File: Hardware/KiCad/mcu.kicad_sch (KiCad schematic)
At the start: 9 parts, among them U3 STM32F427ZGTx, Y1 8 MHz, Y2 32 kHz

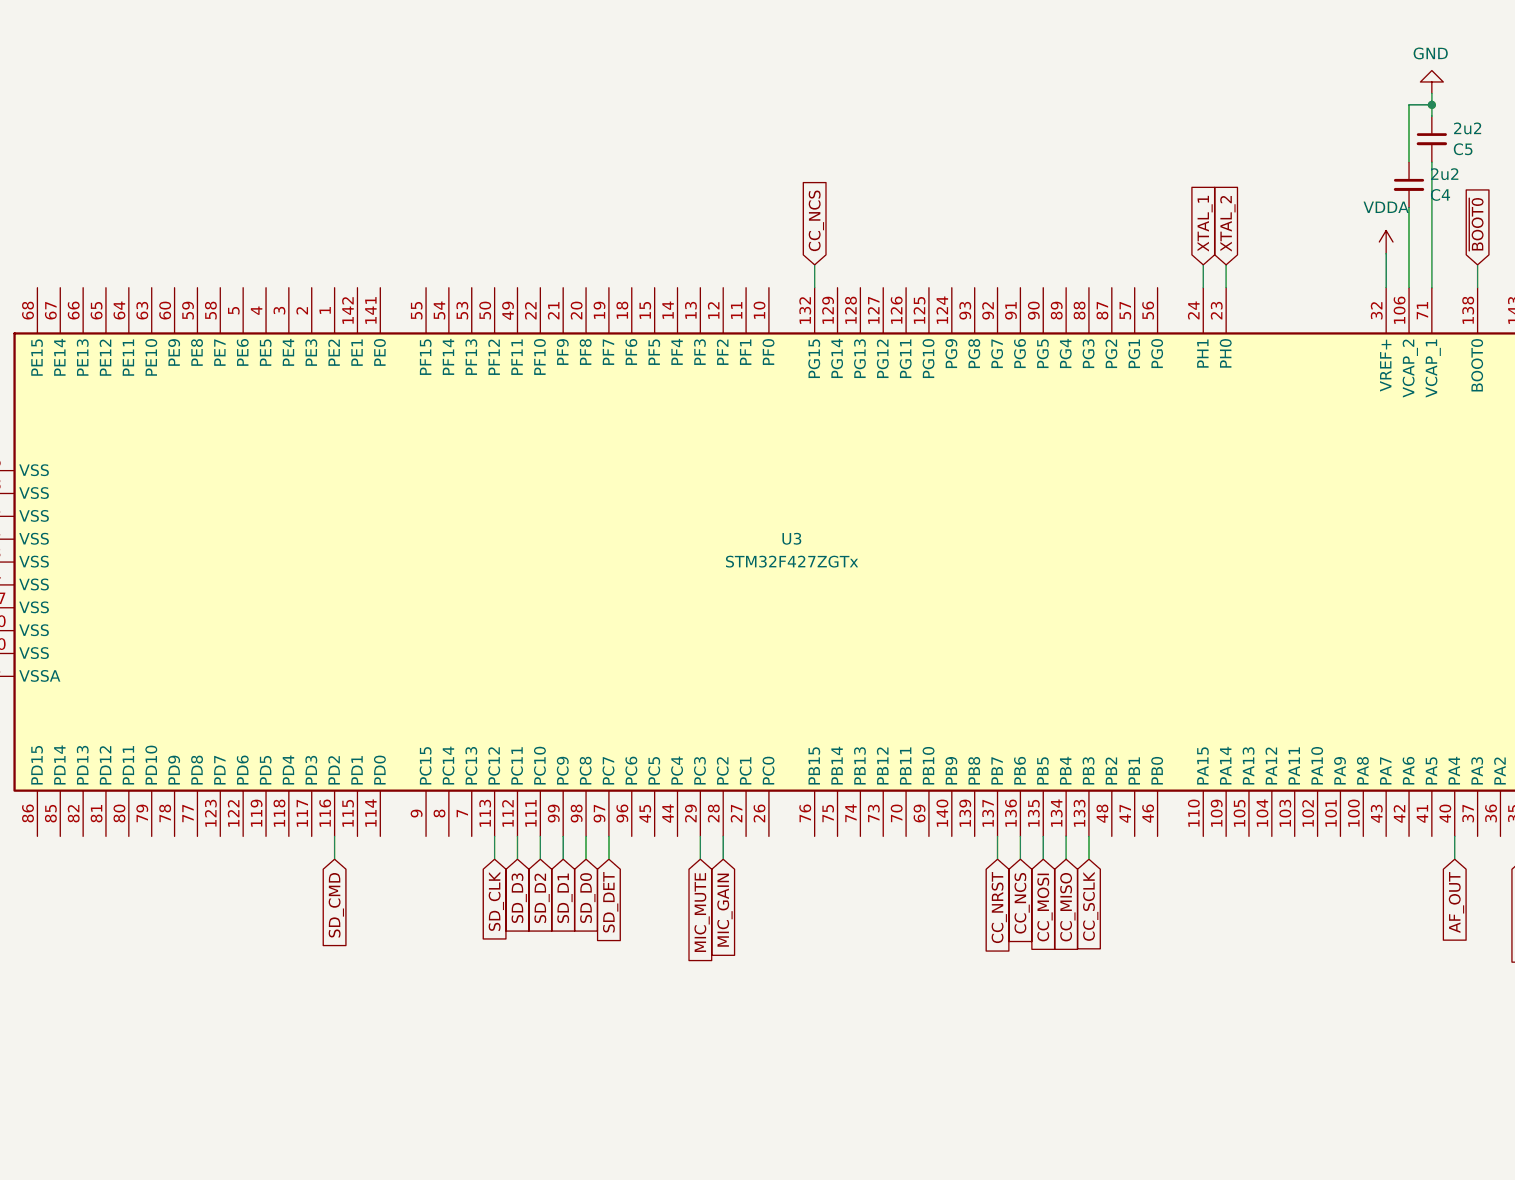
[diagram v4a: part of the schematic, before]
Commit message: add MCU pinouts & add STM .ioc file
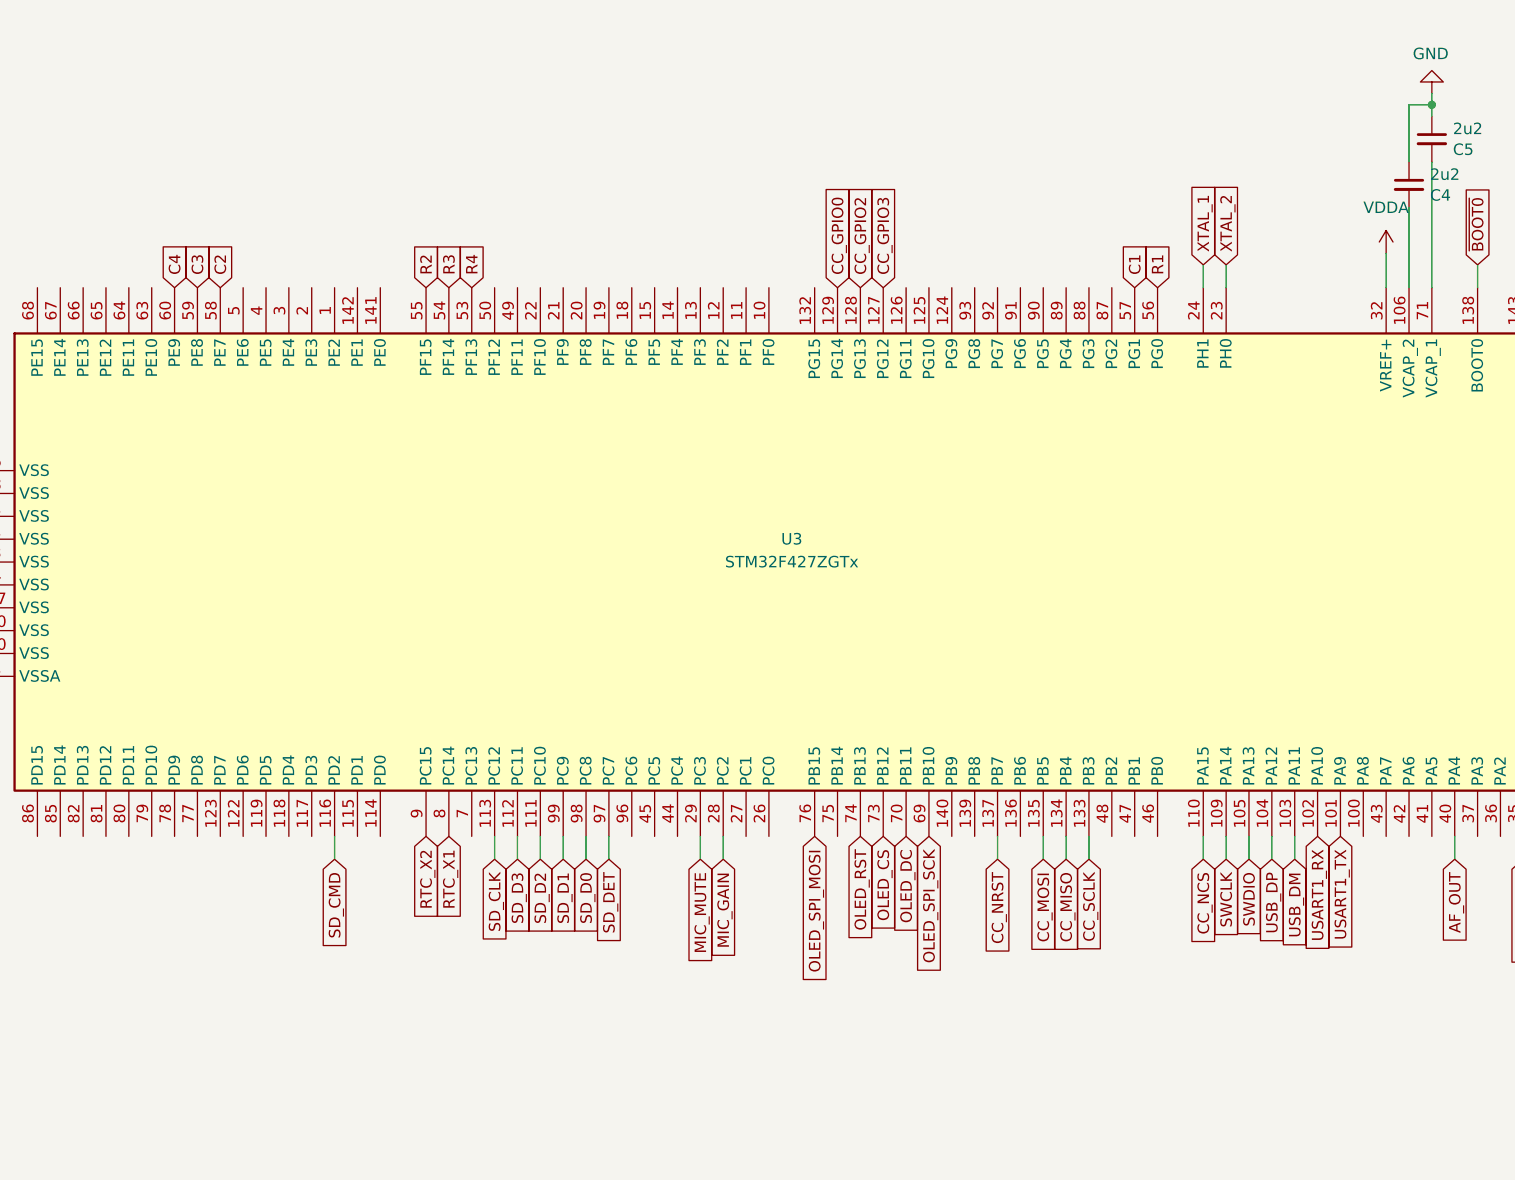
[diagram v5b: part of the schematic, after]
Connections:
- net CC_NCS: now also U3.110 (PA15); no longer U3.132 (PG15), U3.136 (PB6)
- net RTC_X1: now also U3.8 (PC14)
- net RTC_X2: now also U3.9 (PC15)
- net USART1_TX: now reaches U3.101 (PA9)
- net USART1_RX: now reaches U3.102 (PA10)
- net USB_DM: now reaches U3.103 (PA11)
- net USB_DP: now reaches U3.104 (PA12)
- net SWDIO: now reaches U3.105 (PA13)
- net SWCLK: now reaches U3.109 (PA14)
- net CC_GPIO3: now reaches U3.127 (PG12)
- net CC_GPIO2: now reaches U3.128 (PG13)
- net CC_GPIO0: now reaches U3.129 (PG14)
- net R4: now reaches U3.53 (PF13)
- net R3: now reaches U3.54 (PF14)
- net R2: now reaches U3.55 (PF15)
- net R1: now reaches U3.56 (PG0)
- net C1: now reaches U3.57 (PG1)
- net C2: now reaches U3.58 (PE7)
- net C3: now reaches U3.59 (PE8)
- net C4: now reaches U3.60 (PE9)
- net OLED_SPI_SCK: now reaches U3.69 (PB10)
- net OLED_DC: now reaches U3.70 (PB11)
- net OLED_CS: now reaches U3.73 (PB12)
- net OLED_RST: now reaches U3.74 (PB13)
- net OLED_SPI_MOSI: now reaches U3.76 (PB15)

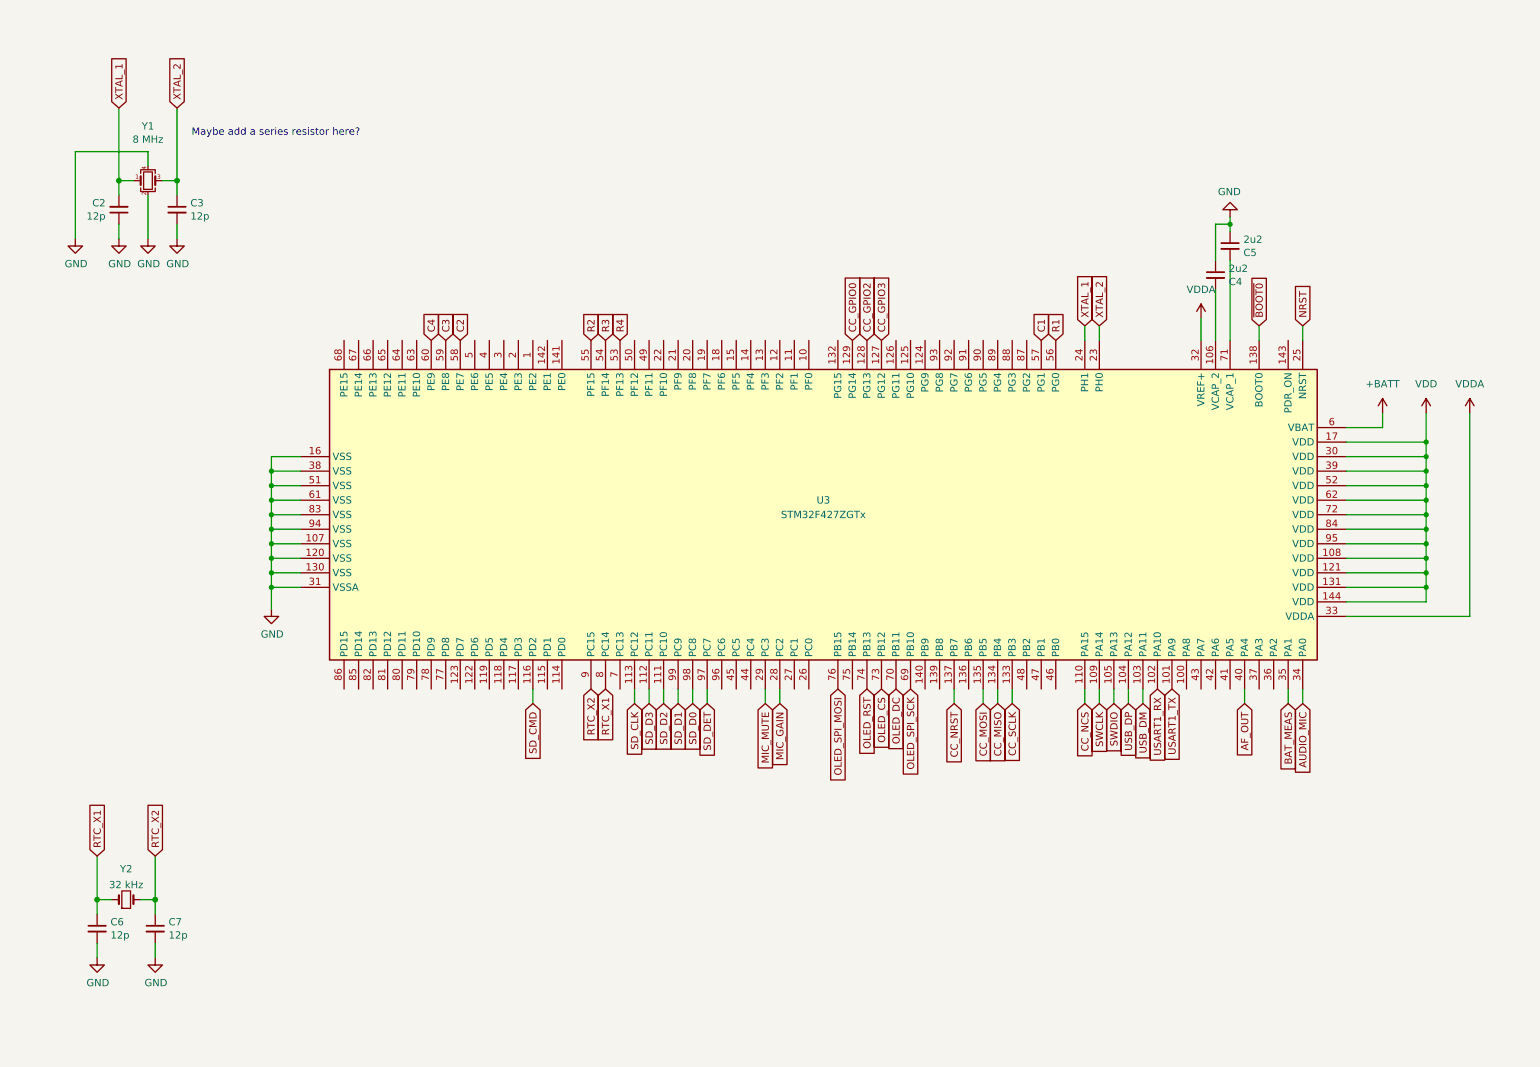
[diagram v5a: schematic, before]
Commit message: move cc1200 spi to spi-5 & update other labels throughout
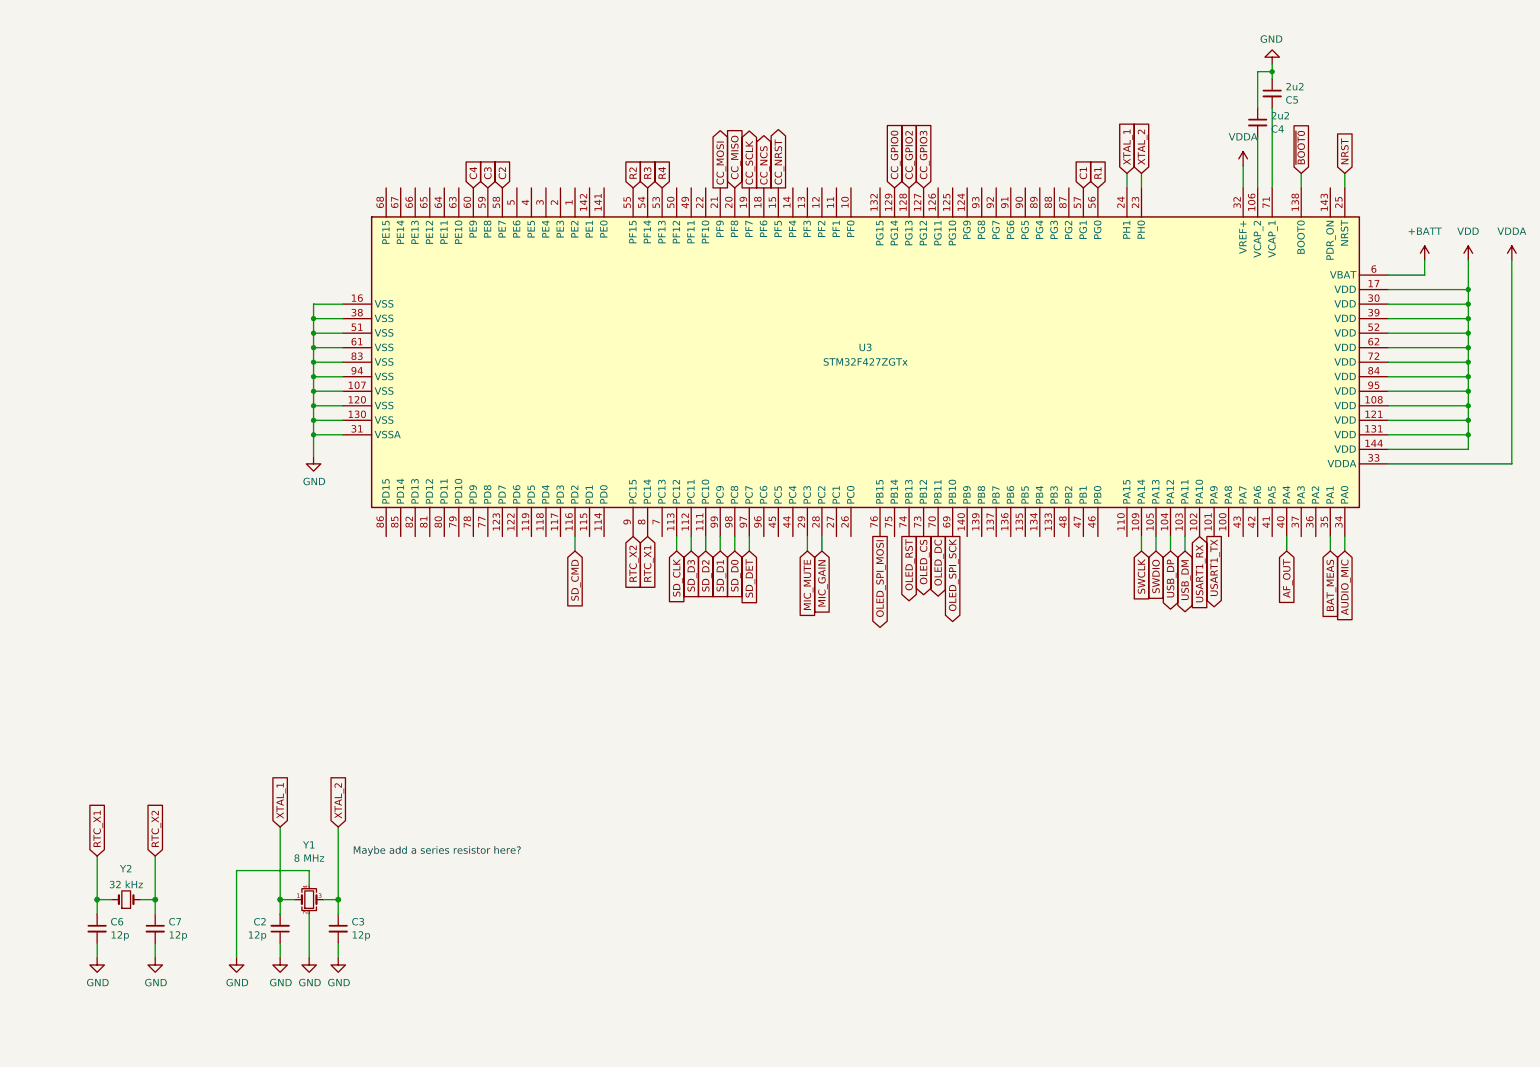
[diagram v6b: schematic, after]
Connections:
- net CC_MISO: now also U3.20 (PF8); no longer U3.134 (PB4)
- net CC_MOSI: now also U3.21 (PF9); no longer U3.135 (PB5)
- net CC_NCS: now also U3.18 (PF6); no longer U3.110 (PA15)
- net CC_NRST: now also U3.15 (PF5); no longer U3.137 (PB7)
- net CC_SCLK: now also U3.19 (PF7); no longer U3.133 (PB3)
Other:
- moved on the sheet: C2, C3, C4, C5, U3, Y1

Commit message: rough layout of cc1200
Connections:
- net +BATT renamed VBAT
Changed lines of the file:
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@@
     (stroke (width 0) (type solid) (color 0 0 0 0))
+  )
+  (wire (pts (xy 260.096 57.15) (xy 260.096 59.69))
+    (stroke (width 0) (type default) (color 0 0 0 0))
   )
   (wire (pts (xy 65.786 67.31) (xy 65.786 64.77))
@@
   )
   (wire (pts (xy 65.786 87.63) (xy 70.866 87.63))
-    (stroke (width 0) (type default) (color 0 0 0 0))
-  )
-  (wire (pts (xy 260.096 57.15) (xy 260.096 59.69))
     (stroke (width 0) (type default) (color 0 0 0 0))
   )
@@
     (pin "99")
   )
-  (symbol (lib_id "power:+BATT") (at 260.096 57.15 0) (unit 1)
-    (in_bom yes) (on_board yes) (fields_autoplaced)
-    (property "Reference" "#PWR0103" (id 0) (at 260.096 60.96 0)
-      (effects (font (size 1.27 1.27)) hide)
-    )
-    (property "Value" "+BATT" (id 1) (at 260.096 52.07 0))
-    (property "Footprint" "" (id 2) (at 260.096 57.15 0)
-      (effects (font (size 1.27 1.27)) hide)
-    )
-    (property "Datasheet" "" (id 3) (at 260.096 57.15 0)
-      (effects (font (size 1.27 1.27)) hide)
-    )
-    (pin "1")
-  )
   (symbol (lib_id "power:VDDA") (at 275.336 57.15 0) (unit 1)
     (in_bom yes) (on_board yes) (fields_autoplaced)
@@
     (pin "2")
   )
+  (symbol (lib_id "pkl_power:VBAT") (at 260.096 57.15 0) (unit 1)
+    (in_bom yes) (on_board yes) (fields_autoplaced)
+    (property "Reference" "#PWR0103" (id 0) (at 260.096 60.96 0)
+      (effects (font (size 1.27 1.27)) hide)
+    )
+    (property "Value" "RTC_BAT" (id 1) (at 256.286 53.34 0)
+      (effects (font (size 1.27 1.27)) (justify left))
+    )
+    (property "Footprint" "" (id 2) (at 260.096 57.15 0)
+      (effects (font (size 1.27 1.27)) hide)
+    )
+    (property "Datasheet" "" (id 3) (at 260.096 57.15 0)
+      (effects (font (size 1.27 1.27)) hide)
+    )
+    (pin "1")
+  )
   (symbol (lib_id "power:VDD") (at 267.716 57.15 0) (unit 1)
